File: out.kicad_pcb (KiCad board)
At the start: 4 copper layers, 30 x 128.5 mm, 77 parts, among them J1 IN_L, J2 POWER, J3 IN_R, J4 IN_CUE, J5 STEREO_OUT, J6 PHONE_OUT, Q1 MMBT3904, Q2 MMBT3904, Q3 MMBT3904, SW1 PHONE_SELECTOR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

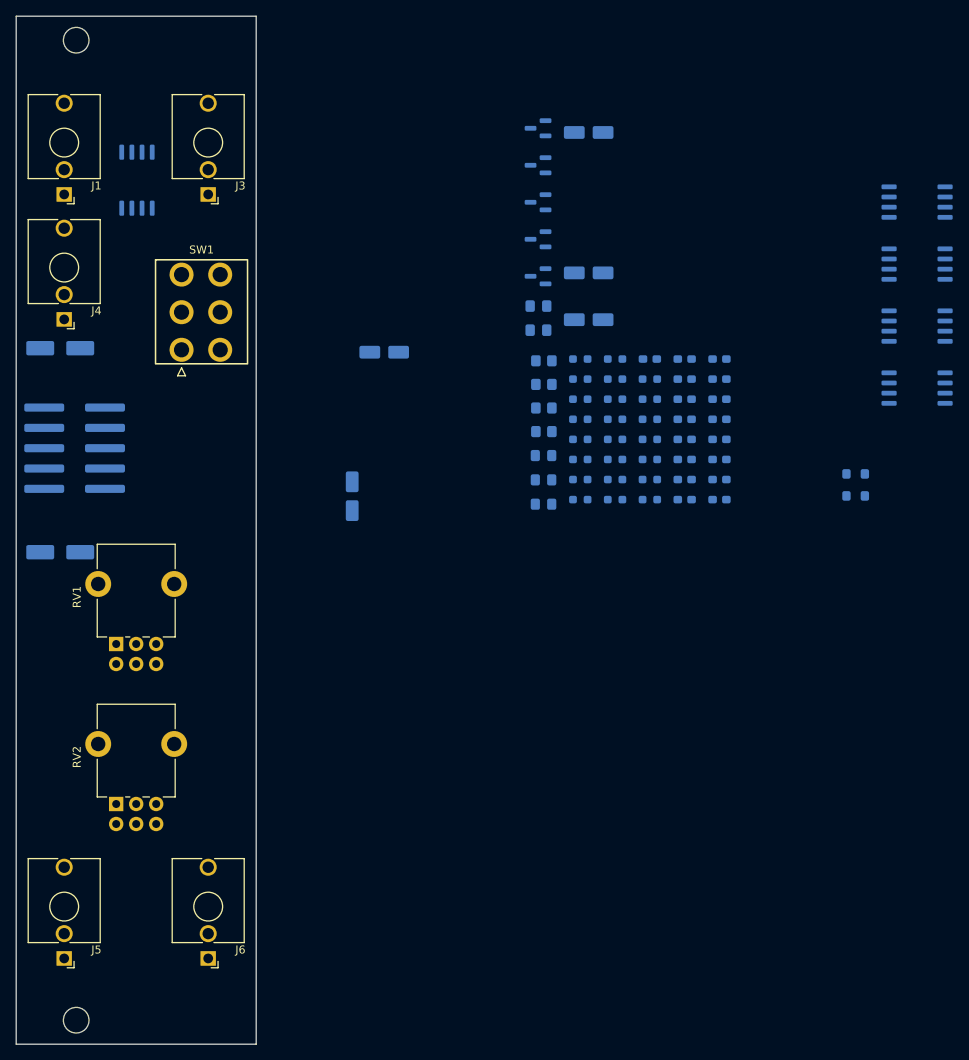
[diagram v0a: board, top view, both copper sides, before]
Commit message: feat: route power planes
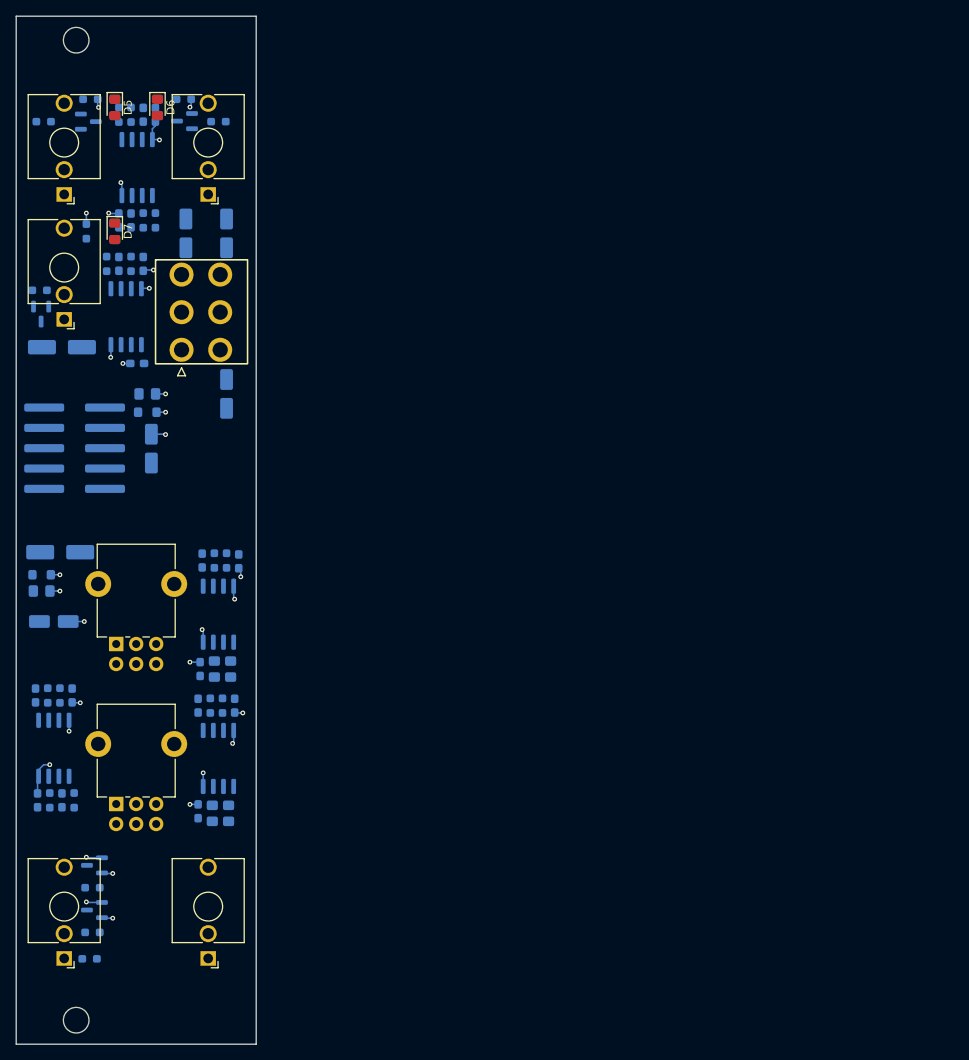
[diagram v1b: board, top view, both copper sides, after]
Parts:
- D5, D6, D7: moved to F.Cu
- moved U3 123.7 mm to (44.7, 121.5), turned to -90 degrees
- moved D4 108.4 mm to (49.8, 141.7)
- moved D3 107.5 mm to (49.8, 136.1)
- moved FB2 102.2 mm to (43.2, 99.8), turned to 0 degrees
- moved U2 99.9 mm to (53.7, 67.6), turned to -90 degrees
- moved U5 98.8 mm to (65.3, 122.8), turned to -90 degrees
- moved U4 94.5 mm to (65.3, 104.7), turned to -90 degrees
- moved C15 93.2 mm to (42.7, 128.0), turned to 90 degrees
- moved C19 91.3 mm to (45.7, 128.0), turned to 90 degrees
- moved R13 90.6 mm to (49.2, 147.8), turned to 0 degrees
- moved C17 90.3 mm to (42.4, 114.9), turned to 90 degrees
- moved R12 89.8 mm to (49.5, 144.5), turned to 0 degrees
- moved FB1 88.9 mm to (56.4, 79.5), turned to 0 degrees
- moved R11 87.7 mm to (49.5, 138.9), turned to 0 degrees
- moved C16 87.4 mm to (47.0, 114.9), turned to -90 degrees
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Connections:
- D3 pad 1: -12V -> +12VA
- D3 pad 2: +12V -> -12VA
- D4 pad 1: -12V -> +12VA
- D4 pad 2: +12V -> -12VA
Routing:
- net -12VA: track 0.00 -> 203.3 mm, vias 0 -> 15
- net +12VA: track 0.00 -> 187.7 mm, vias 0 -> 16
- added copper zone on In1.Cu, net +12VA
- added copper zone on In1.Cu, net -12VA
- added copper zone on In2.Cu, net GND

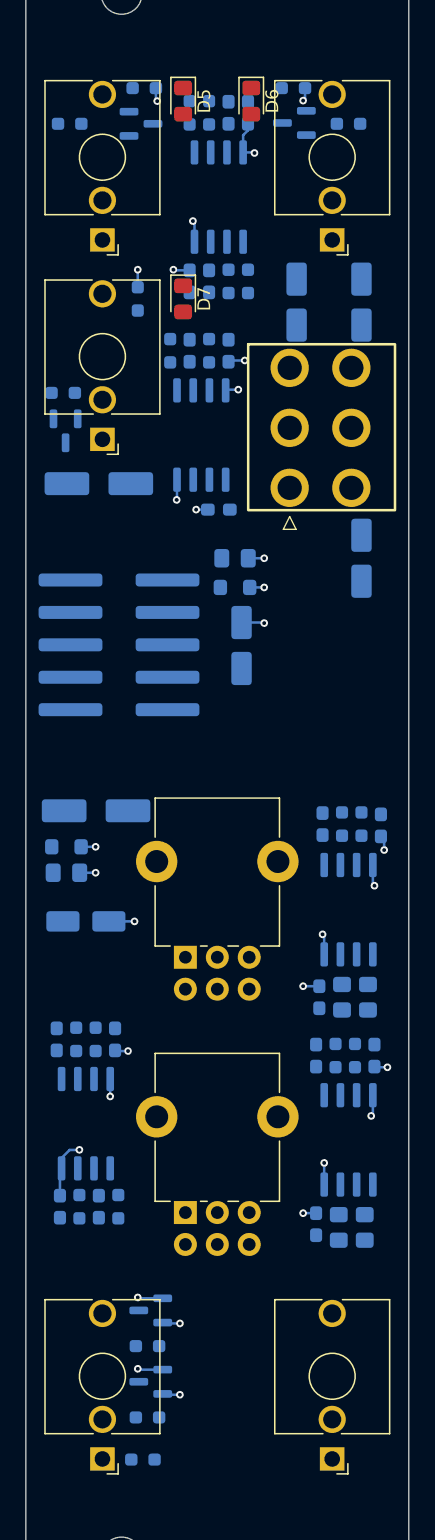
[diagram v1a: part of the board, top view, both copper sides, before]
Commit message: pcb: signal tracks
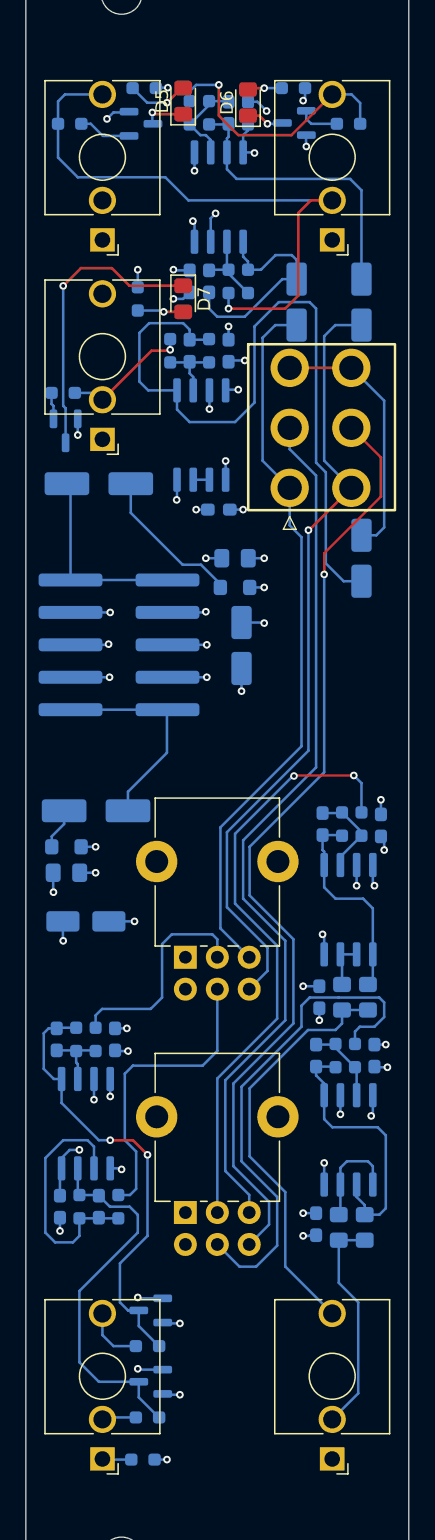
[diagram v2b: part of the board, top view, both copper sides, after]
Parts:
- moved D6 0.28 mm to (57.4, 41.5), turned to 90 degrees
- turned D5 to 90 degrees
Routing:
- net Net-(SW1B-B): track 0.00 -> 74.4 mm, vias 0 -> 1
- net Net-(SW1A-B): track 0.00 -> 68.8 mm
- net Net-(SW1B-A): track 0.00 -> 61.3 mm, vias 0 -> 1
- net Net-(C11-Pad2): track 0.00 -> 57.9 mm
- net Net-(SW1A-A): track 0.00 -> 56.4 mm
- net GND: track 0.00 -> 53.3 mm, vias 0 -> 32
- net IN_L: track 0.00 -> 47.6 mm, vias 0 -> 1
- net Net-(R14-Pad2): track 0.00 -> 47.3 mm, vias 0 -> 2
- net Net-(R16-Pad2): track 0.00 -> 39.8 mm
- net Net-(D3-COM): track 0.00 -> 35.2 mm, vias 0 -> 2
- net Net-(J6-PadT): track 0.00 -> 32.7 mm
- net Net-(D4-COM): track 0.00 -> 29.6 mm
- net Net-(R9-Pad2): track 0.00 -> 23.8 mm
- net Net-(C10-Pad1): track 0.00 -> 23.3 mm
- net Net-(D7-K): track 0.00 -> 22.9 mm, vias 0 -> 1
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
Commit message: wip: routing
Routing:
- net -12VA: track 205.0 -> 207.1 mm
- net +12VA: track 187.0 -> 188.1 mm
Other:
- board text added: "CUE"
- board text added: "L(M)"
- board text added: "OUTPUT"
- board text added: "PHONE"
- board text added: "R"
- board text added: "RAW SERIES"

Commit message: wip: layout
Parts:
- added G***: LOGO, LOGO, F.Cu at (62.9, 81.3)

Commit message: fix: increase width of input voltage lines
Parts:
- moved C2 2.29 mm to (56.4, 79.5)
- moved FB1 2.29 mm to (56.4, 77.2)
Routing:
- net Net-(D8-K): track 11.9 -> 10.7 mm
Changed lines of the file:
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@@
 			(plot_on_all_layers_selection 0x00000000_00000000_00000000_00000000)
 			(disableapertmacros no)
-			(usegerberextensions no)
-			(usegerberattributes yes)
-			(usegerberadvancedattributes yes)
+			(usegerberextensions yes)
+			(usegerberattributes no)
+			(usegerberadvancedattributes no)
 			(creategerberjobfile yes)
 			(dashed_line_dash_ratio 12.000000)
@@
 			(sketchdnponfab yes)
 			(crossoutdnponfab yes)
-			(subtractmaskfromsilk no)
+			(subtractmaskfromsilk yes)
 			(outputformat 1)
 			(mirror no)
-			(drillshape 1)
+			(drillshape 0)
 			(scaleselection 1)
-			(outputdirectory "")
+			(outputdirectory "output/")
 		)
 	)
@@
 	(footprint "Capacitor_SMD:C_0805_2012Metric_Pad1.18x1.45mm_HandSolder"
 		(layer "B.Cu")
-		(at 56.388 77.216 180)
+		(at 56.388 79.502 180)
 		(descr "Capacitor SMD 0805 (2012 Metric), square (rectangular) end terminal, IPC-7351 nominal with elongated pad for handsoldering. (Body size source: IPC-SM-782 page 76, https://www.pcb-3d.com/wordpress/wp-content/uploads/ipc-sm-782a_amendment_1_and_2.pdf, https://docs.google.com/spreadsheets/d/1BsfQQcO9C6DZCsRaXUlFlo91Tg2WpOkGARC1WS5S8t0/edit?usp=sharing), generated with kicad-footprint-generator")
 		(tags "capacitor handsolder")
@@
 	(footprint "Inductor_SMD:L_0805_2012Metric_Pad1.05x1.20mm_HandSolder"
 		(layer "B.Cu")
-		(at 56.388 79.502)
+		(at 56.388 77.216)
 		(descr "Inductor SMD 0805 (2012 Metric), square (rectangular) end terminal, IPC-7351 nominal with elongated pad for handsoldering. (Body size source: IPC-SM-782 page 80, https://www.pcb-3d.com/wordpress/wp-content/uploads/ipc-sm-782a_amendment_1_and_2.pdf), generated with kicad-footprint-generator")
 		(tags "inductor handsolder")
@@
 	)
 	(gr_line
-		(start 59.436 93.98)
+		(start 59.538929 93.98)
 		(end 64.008 93.98)
 		(stroke
@@
 	)
 	(via
-		(at 54.102 77.216)
-		(size 0.6)
-		(drill 0.3)
-		(layers "F.Cu" "B.Cu")
-		(net 2)
-	)
-	(via
 		(at 44.069 67.564)
 		(size 0.6)
@@
 		(net 2)
 	)
+	(via
+		(at 53.975 80.01)
+		(size 0.6)
+		(drill 0.3)
+		(layers "F.Cu" "B.Cu")
+		(net 2)
+	)
 	(segment
 		(start 55.88 60.0975)
@@
 	)
 	(segment
+		(start 54.483 79.502)
+		(end 53.975 80.01)
+		(width 0.5)
+		(layer "B.Cu")
+		(net 2)
+	)
+	(segment
 		(start 42.904 107.166)
 		(end 42.926 107.188)
@@
 	)
 	(segment
-		(start 55.3505 77.216)
-		(end 54.102 77.216)
-		(width 0.5)
-		(layer "B.Cu")
-		(net 2)
-	)
-	(segment
 		(start 58.137362 41.455)
 		(end 57.404 41.455)
@@
 	)
 	(segment
+		(start 55.3505 79.502)
+		(end 54.483 79.502)
+		(width 0.5)
+		(layer "B.Cu")
+		(net 2)
+	)
+	(segment
 		(start 42.672 128.8785)
 		(end 42.672 129.921)
@@
 	)
 	(segment
-		(start 42.03 99.0035)
-		(end 43 98.0335)
-		(width 0.2)
+		(start 43 97.843)
+		(end 42.03 98.813)
+		(width 0.5)
 		(layer "B.Cu")
 		(net 22)
 	)
 	(segment
-		(start 43 98.0335)
-		(end 43 97)
-		(width 0.2)
+		(start 42.03 98.813)
+		(end 42.03 99.822)
+		(width 0.5)
 		(layer "B.Cu")
 		(net 22)
 	)
 	(segment
-		(start 42.03 99.822)
-		(end 42.03 99.0035)
-		(width 0.2)
+		(start 43 97)
+		(end 43 97.843)
+		(width 0.5)
 		(layer "B.Cu")
 		(net 22)
@@
 	)
 	(segment
-		(start 52.284 77.724)
-		(end 48.22 73.66)
-		(width 0.2)
+		(start 55.238 77.216)
+		(end 51.943 77.216)
+		(width 0.5)
 		(layer "B.Cu")
 		(net 30)
 	)
 	(segment
-		(start 55.238 79.241)
-		(end 53.721 77.724)
-		(width 0.2)
+		(start 51.943 77.216)
+		(end 48.22 73.493)
+		(width 0.5)
 		(layer "B.Cu")
 		(net 30)
 	)
 	(segment
-		(start 48.22 73.66)
+		(start 48.22 73.493)
 		(end 48.22 71.374)
-		(width 0.2)
-		(layer "B.Cu")
-		(net 30)
-	)
-	(segment
-		(start 55.238 79.502)
-		(end 55.238 79.241)
-		(width 0.2)
-		(layer "B.Cu")
-		(net 30)
-	)
-	(segment
-		(start 53.721 77.724)
-		(end 52.284 77.724)
-		(width 0.2)
+		(width 0.5)
 		(layer "B.Cu")
 		(net 30)

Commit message: fix: correct errors found in release 1.0.0
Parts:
- removed D3, D4: BAT54S, Package_TO_SOT_SMD:SOT-23
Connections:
- C24 pad 1: Net-(U5A-+) -> Net-(U5A--)
- C24 pad 2: Net-(U5B--) -> Net-(U5B-+)
- J4 pad T: unconnected-(J4-PadT) -> IN_CUE
- J4 pad TN: IN_CUE -> unconnected-(J4-PadTN)
- R16 pad 1: Net-(U5A-+) -> Net-(U5A--)
- R17 pad 1: Net-(U5B--) -> Net-(U5B-+)
- R17 pad 2: Net-(U5A-+) -> Net-(U5A--)
- R18 pad 2: Net-(U5B-+) -> Net-(U5B--)
- R19 pad 2: Net-(U5B--) -> Net-(U5B-+)
- U5 pad 1: Net-(U5B--) -> Net-(U5B-+)
- U5 pad 2: GND -> Net-(U5A--)
- U5 pad 3: Net-(U5A-+) -> GND
- U5 pad 7: Net-(U5B-+) -> Net-(U5B--)
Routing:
- net Net-(U5B--): track 21.5 -> 3.68 mm
- net Net-(U5B-+): track 8.07 -> 21.5 mm
- net IN_CUE: track 10.2 -> 17.5 mm
- net Net-(U5A--): track 0.00 -> 6.85 mm
- net Net-(U5A-+): track 6.25 -> 0.00 mm
- net -12VA: track 207.1 -> 207.7 mm, vias 15 -> 14

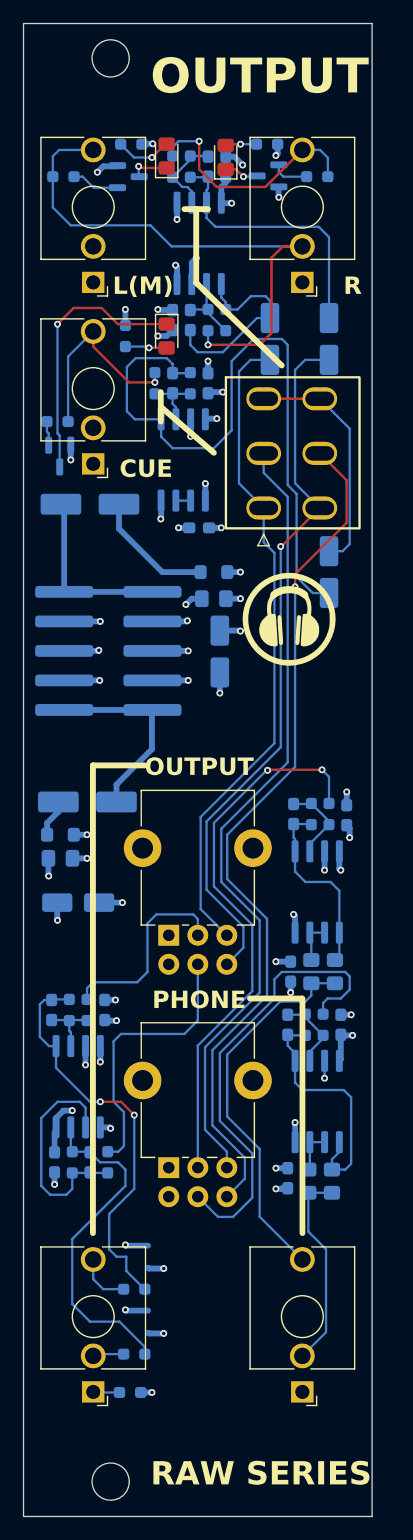
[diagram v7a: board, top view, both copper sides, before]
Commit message: feat: adapt pcb to two layers, fix opamp and jack routing
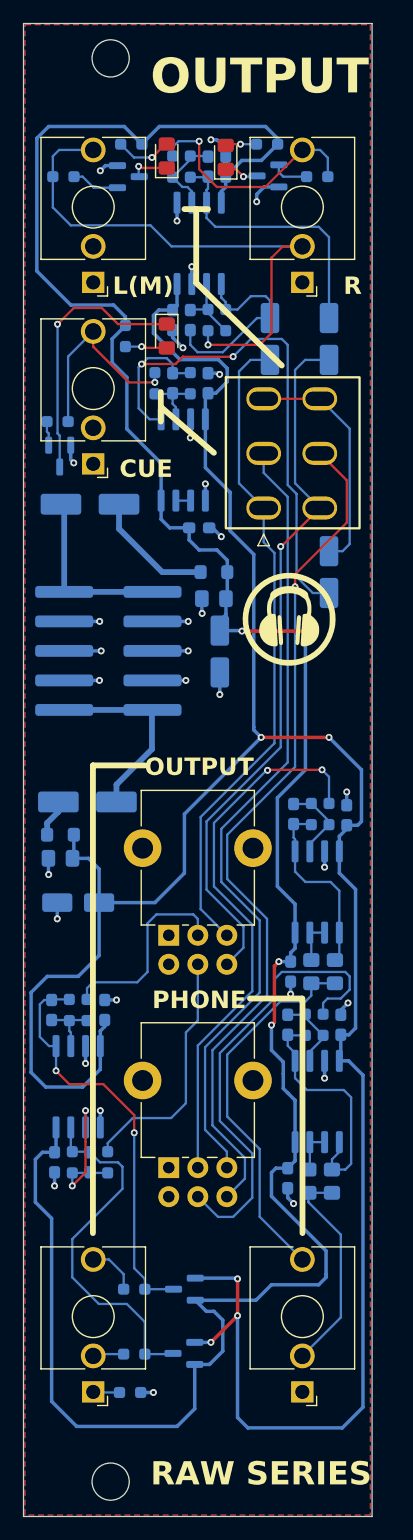
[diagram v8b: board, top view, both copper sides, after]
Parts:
- added D2: BAT54S, Package_TO_SOT_SMD:SOT-23, B.Cu at (53.8, 138.9)
- added D3: BAT54S, Package_TO_SOT_SMD:SOT-23, B.Cu at (53.8, 144.5)
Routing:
- net +12VA: track 188.1 -> 220.1 mm, vias 16 -> 4
- net Net-(C11-Pad2): track 57.9 -> 49.0 mm, vias 0 -> 2
- net Net-(U3B--): track 19.8 -> 12.6 mm, vias 0 -> 2
- net GND: track 53.6 -> 57.2 mm
- net Net-(R9-Pad2): track 23.8 -> 21.3 mm
- net Net-(D3-COM): track 29.2 -> 31.4 mm
- net -12VA: track 207.7 -> 209.8 mm, vias 14 -> 5
- net Net-(J6-PadR): track 17.5 -> 18.6 mm
- added copper zone on F.Cu, net GND
- removed copper zone on In1.Cu, net +12VA
- removed copper zone on In1.Cu, net -12VA
- removed copper zone on In2.Cu, net GND
